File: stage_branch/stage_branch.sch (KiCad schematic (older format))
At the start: 1 part, among them P1 DIN_41612_128P

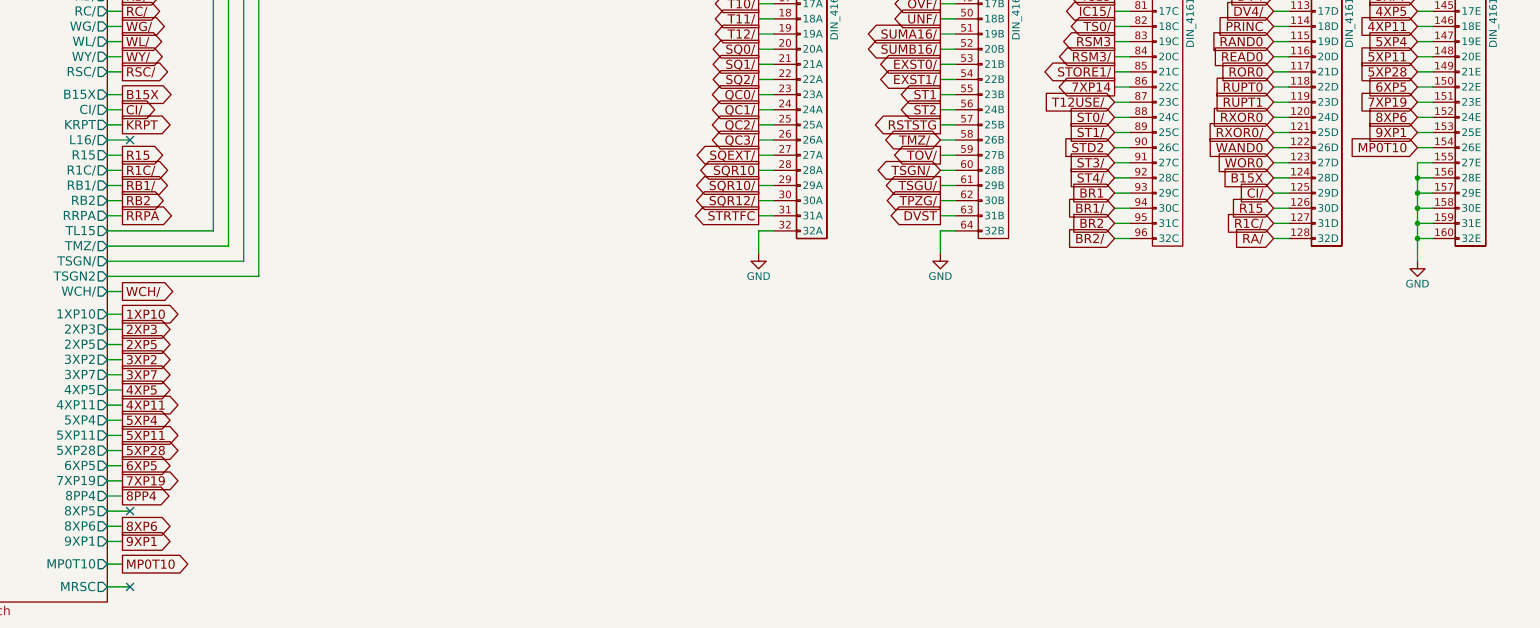
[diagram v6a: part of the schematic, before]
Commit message: Added and tied in module 12, parity & s register
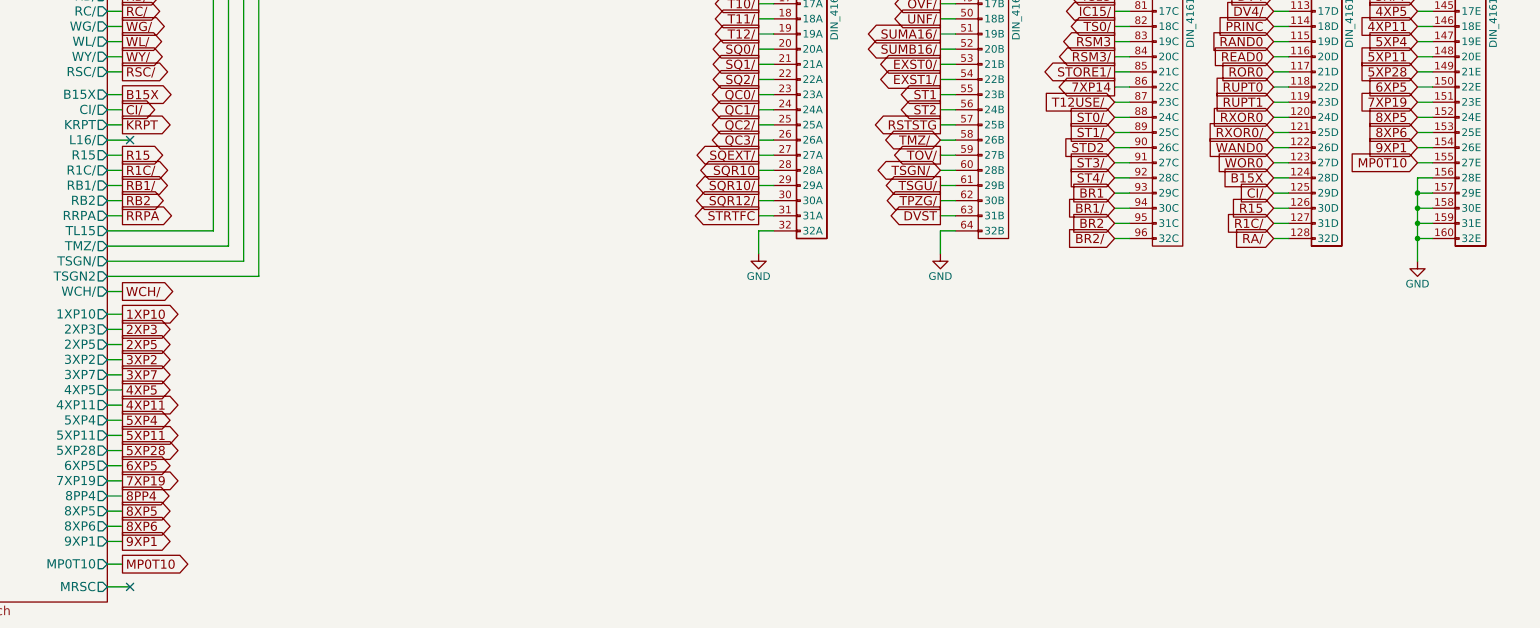
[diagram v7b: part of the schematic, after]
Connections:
- net 8XP6: now also P1.153 (25E); no longer P1.152 (24E)
- net 9XP1: now also P1.154 (26E); no longer P1.153 (25E)
- net GND: no longer P1.155 (27E)
- net MP0T10: now also P1.155 (27E); no longer P1.154 (26E)
- new net 8XP5: P1.152 (24E)
- no-connect marks 25 -> 24
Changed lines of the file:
@@
 Text GLabel 13700 5300 0    60   Output ~ 0
 EXST1/
-NoConn ~ 8350 8150
 Text GLabel 8300 2350 2    60   Output ~ 0
 BR1B2B
@@
 	8300 8050 8200 8050
 Wire Wire Line
-	8200 8150 8350 8150
+	8200 8150 8300 8150
 Wire Wire Line
 	8300 8250 8200 8250
@@
 Connection ~ 16850 6150
 Wire Wire Line
-	16850 5850 16950 5850
-Wire Wire Line
 	16850 5950 16950 5950
-Connection ~ 16850 5950
 Wire Wire Line
 	16850 6050 16950 6050
@@
 Text GLabel 8300 8500 2    60   Output ~ 0
 MP0T10
-Text GLabel 16850 5750 0    60   Input ~ 0
+Text GLabel 16850 5850 0    60   Input ~ 0
 MP0T10
 Wire Wire Line
-	16850 5750 16950 5750
+	16850 5850 16950 5850
 Text GLabel 8300 5800 2    60   Output ~ 0
 R15
@@
 Text GLabel 8300 8250 2    60   Output ~ 0
 8XP6
-Text GLabel 16850 5550 0    60   Input ~ 0
+Text GLabel 16850 5650 0    60   Input ~ 0
 8XP6
 Text GLabel 8300 8350 2    60   Output ~ 0
 9XP1
-Text GLabel 16850 5650 0    60   Input ~ 0
+Text GLabel 16850 5750 0    60   Input ~ 0
 9XP1
 Wire Wire Line
@@
 	16850 5450 16950 5450
 Wire Wire Line
-	16950 5550 16850 5550
-Wire Wire Line
-	16850 5650 16950 5650
-Wire Wire Line
-	16850 5850 16850 6500
+	16950 5650 16850 5650
+Wire Wire Line
+	16850 5750 16950 5750
+Wire Wire Line
+	16850 5950 16850 6500
 Text GLabel 8300 7350 2    60   Output ~ 0
 4XP5
@@
 Text GLabel 16850 4150 0    60   Input ~ 0
 WY/
+Text GLabel 8300 8150 2    60   Output ~ 0
+8XP5
+Text GLabel 16850 5550 0    60   Input ~ 0
+8XP5
+Wire Wire Line
+	16950 5550 16850 5550
 $EndSCHEMATC

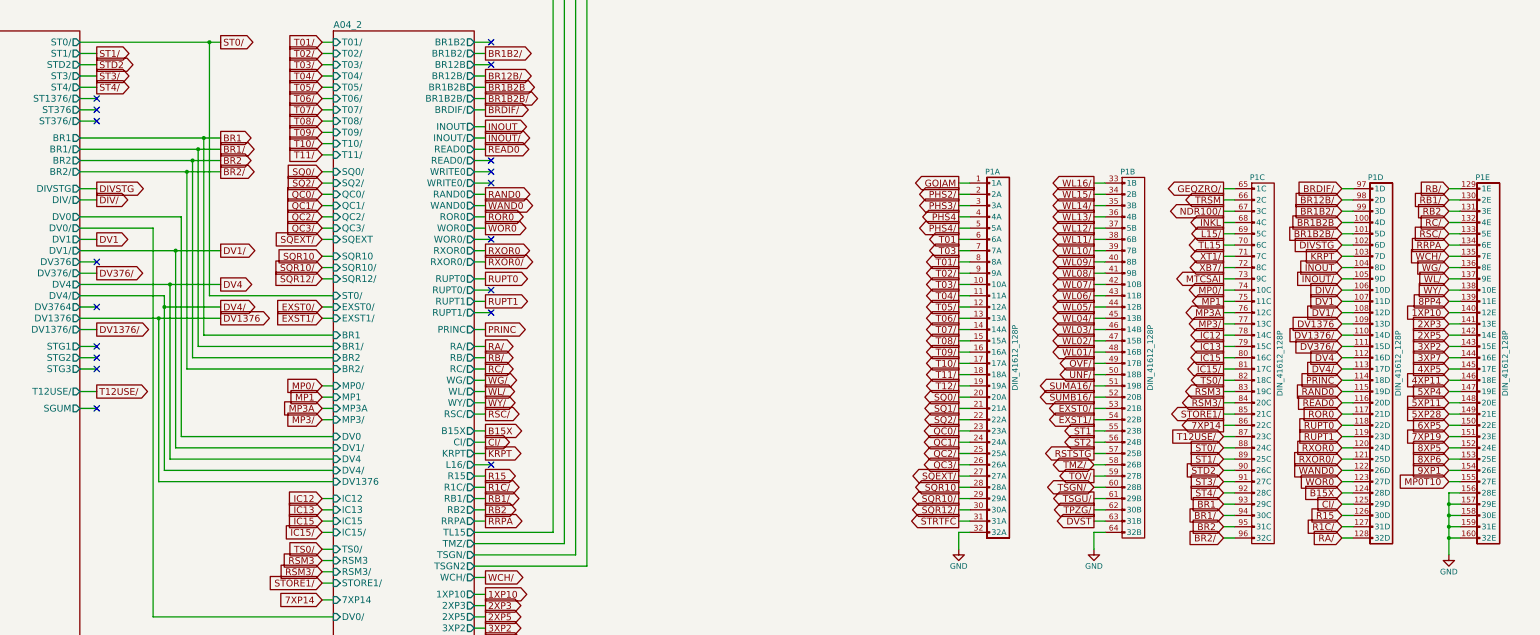
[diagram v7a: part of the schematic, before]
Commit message: Bux fixes for things found during FPGA integration.
* A05 was driving TSGN/ directly instead of with an OD buffer+pullup
* Some bad logic with crosspoints in module 5
* A bad part number in module 12
* Removal of unused signals from the backplane connectors
* Addition of some monitor signals from the timer to the backplane
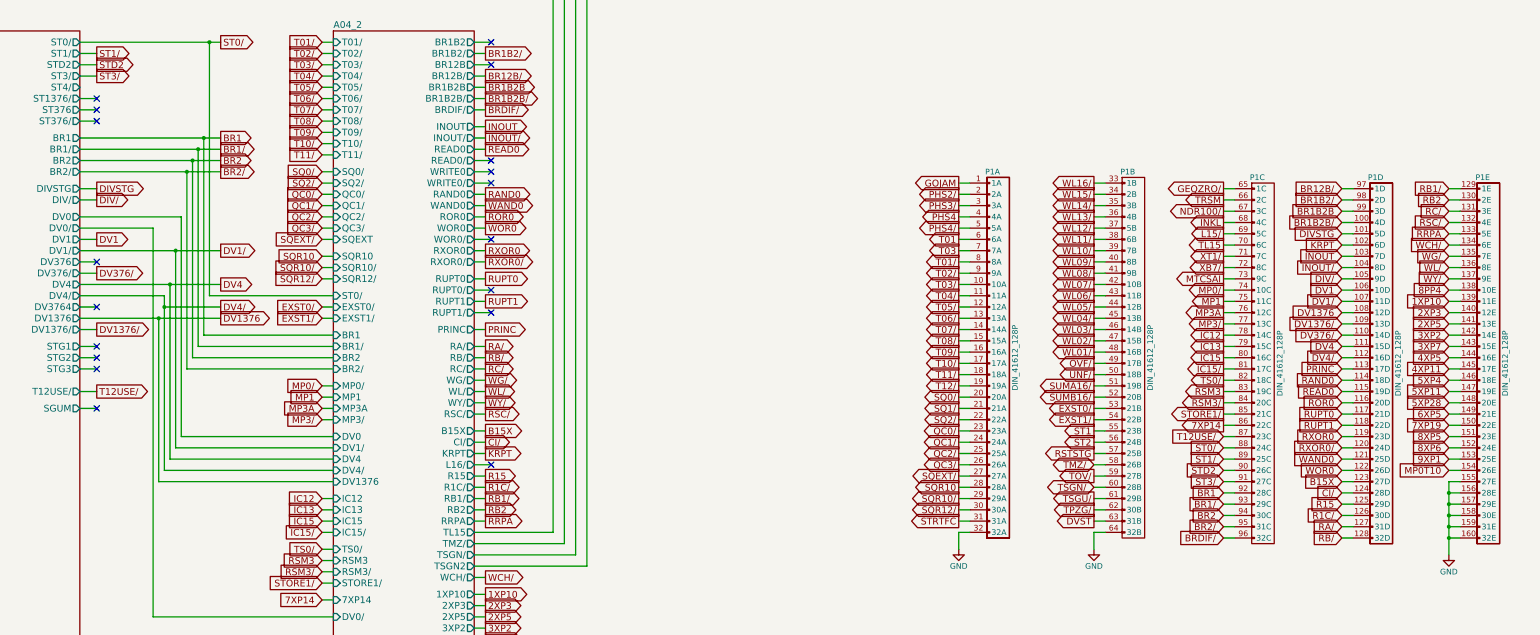
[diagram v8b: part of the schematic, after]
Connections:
- net ST4/ is gone; now on net BR1: P1.92 (28C)
- net 1XP10: now also P1.139 (11E); no longer P1.140 (12E)
- net 2XP3: now also P1.140 (12E); no longer P1.141 (13E)
- net 2XP5: now also P1.141 (13E); no longer P1.142 (14E)
- net 3XP2: now also P1.142 (14E); no longer P1.143 (15E)
- net 3XP7: now also P1.143 (15E); no longer P1.144 (16E)
- net 4XP11: now also P1.145 (17E); no longer P1.146 (18E)
- net 4XP5: now also P1.144 (16E); no longer P1.145 (17E)
- net 5XP11: now also P1.147 (19E); no longer P1.148 (20E)
- net 5XP28: now also P1.148 (20E); no longer P1.149 (21E)
- net 5XP4: now also P1.146 (18E); no longer P1.147 (19E)
- net 6XP5: now also P1.149 (21E); no longer P1.150 (22E)
- net 7XP19: now also P1.150 (22E); no longer P1.151 (23E)
- net 8PP4: now also P1.138 (10E); no longer P1.139 (11E)
- net 8XP5: now also P1.151 (23E); no longer P1.152 (24E)
- net 8XP6: now also P1.152 (24E); no longer P1.153 (25E)
- net 9XP1: now also P1.153 (25E); no longer P1.154 (26E)
- net B15X: now also P1.123 (27D); no longer P1.124 (28D)
- net BR1: no longer P1.93 (29C)
- net BR1/: now also P1.93 (29C); no longer P1.94 (30C)
- net BR12B/: now also P1.97 (1D); no longer P1.98 (2D)
- net BR1B2/: now also P1.98 (2D); no longer P1.99 (3D)
- net BR1B2B: now also P1.99 (3D); no longer P1.100 (4D)
- net BR1B2B/: now also P1.100 (4D); no longer P1.101 (5D)
- net BR2: now also P1.94 (30C); no longer P1.95 (31C)
- net BR2/: now also P1.95 (31C); no longer P1.96 (32C)
- net BRDIF/: now also P1.96 (32C); no longer P1.97 (1D)
- net CI/: now also P1.124 (28D); no longer P1.125 (29D)
- net DIV/: now also P1.105 (9D); no longer P1.106 (10D)
- net DIVSTG: now also P1.101 (5D); no longer P1.102 (6D)
- net DV1: now also P1.106 (10D); no longer P1.107 (11D)
- net DV1/: now also P1.107 (11D); no longer P1.108 (12D)
- net DV1376: now also P1.108 (12D); no longer P1.109 (13D)
- net DV1376/: now also P1.109 (13D); no longer P1.110 (14D)
- net DV376/: now also P1.110 (14D); no longer P1.111 (15D)
- net DV4: now also P1.111 (15D); no longer P1.112 (16D)
- net DV4/: now also P1.112 (16D); no longer P1.113 (17D)
- net GND: now also P1.155 (27E)
- net INOUT: now also P1.103 (7D); no longer P1.104 (8D)
- net INOUT/: now also P1.104 (8D); no longer P1.105 (9D)
- net KRPT: now also P1.102 (6D); no longer P1.103 (7D)
- net MP0T10: now also P1.154 (26E); no longer P1.155 (27E)
- net PRINC: now also P1.113 (17D); no longer P1.114 (18D)
- net R15: now also P1.125 (29D); no longer P1.126 (30D)
- net R1C/: now also P1.126 (30D); no longer P1.127 (31D)
- net RA/: now also P1.127 (31D); no longer P1.128 (32D)
- net RAND0: now also P1.114 (18D); no longer P1.115 (19D)
- net RB/: now also P1.128 (32D); no longer P1.129 (1E)
- net RB1/: now also P1.129 (1E); no longer P1.130 (2E)
- net RB2: now also P1.130 (2E); no longer P1.131 (3E)
- net RC/: now also P1.131 (3E); no longer P1.132 (4E)
- net READ0: now also P1.115 (19D); no longer P1.116 (20D)
- net ROR0: now also P1.116 (20D); no longer P1.117 (21D)
- net RRPA: now also P1.133 (5E); no longer P1.134 (6E)
- net RSC/: now also P1.132 (4E); no longer P1.133 (5E)
- net RUPT0: now also P1.117 (21D); no longer P1.118 (22D)
- net RUPT1: now also P1.118 (22D); no longer P1.119 (23D)
- net RXOR0: now also P1.119 (23D); no longer P1.120 (24D)
- net RXOR0/: now also P1.120 (24D); no longer P1.121 (25D)
- net WAND0: now also P1.121 (25D); no longer P1.122 (26D)
- net WCH/: now also P1.134 (6E); no longer P1.135 (7E)
- net WG/: now also P1.135 (7E); no longer P1.136 (8E)
- net WL/: now also P1.136 (8E); no longer P1.137 (9E)
- net WOR0: now also P1.122 (26D); no longer P1.123 (27D)
- net WY/: now also P1.137 (9E); no longer P1.138 (10E)
